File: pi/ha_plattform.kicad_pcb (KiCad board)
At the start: 2 copper layers, 54 x 55 mm, 15 parts, among them J3 Raspberry_Pi_2_3

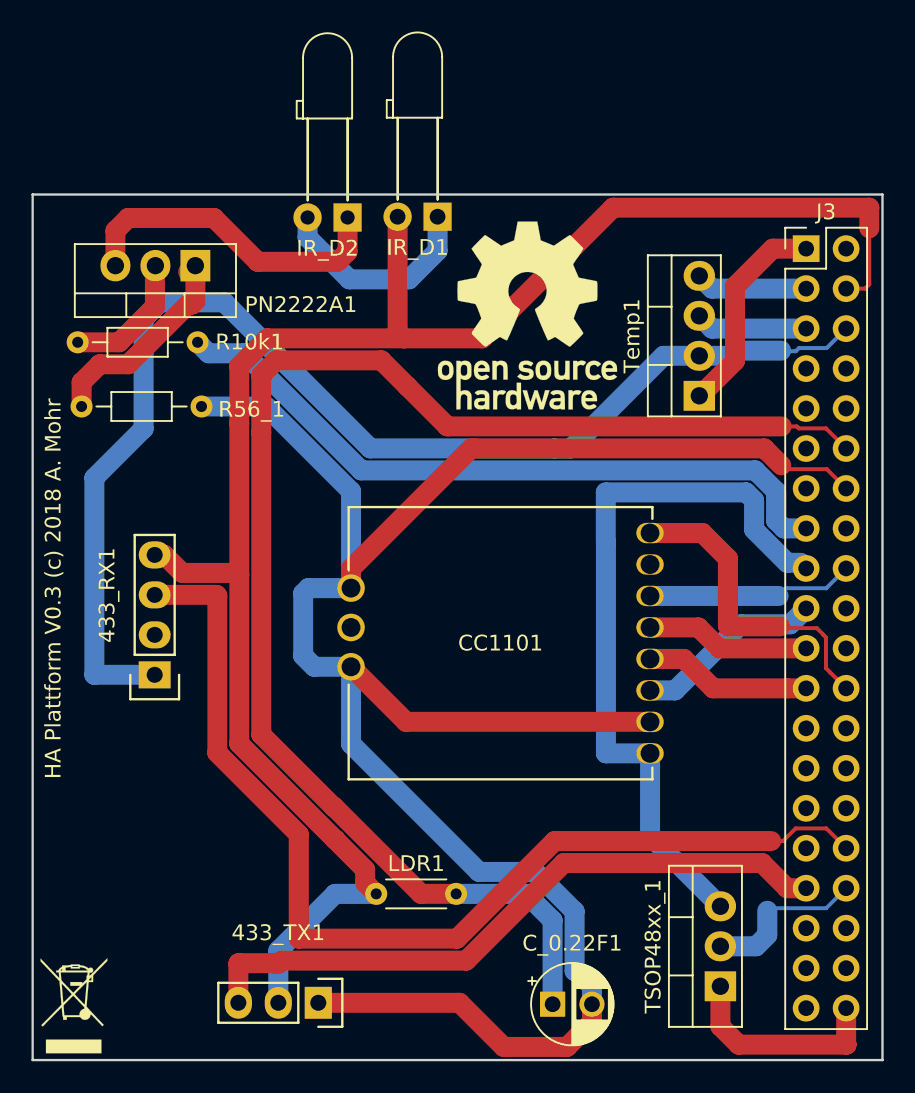
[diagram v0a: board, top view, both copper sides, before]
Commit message: Rerouted because footprints of 433mhz rx/tx were wrong-32-51.sch
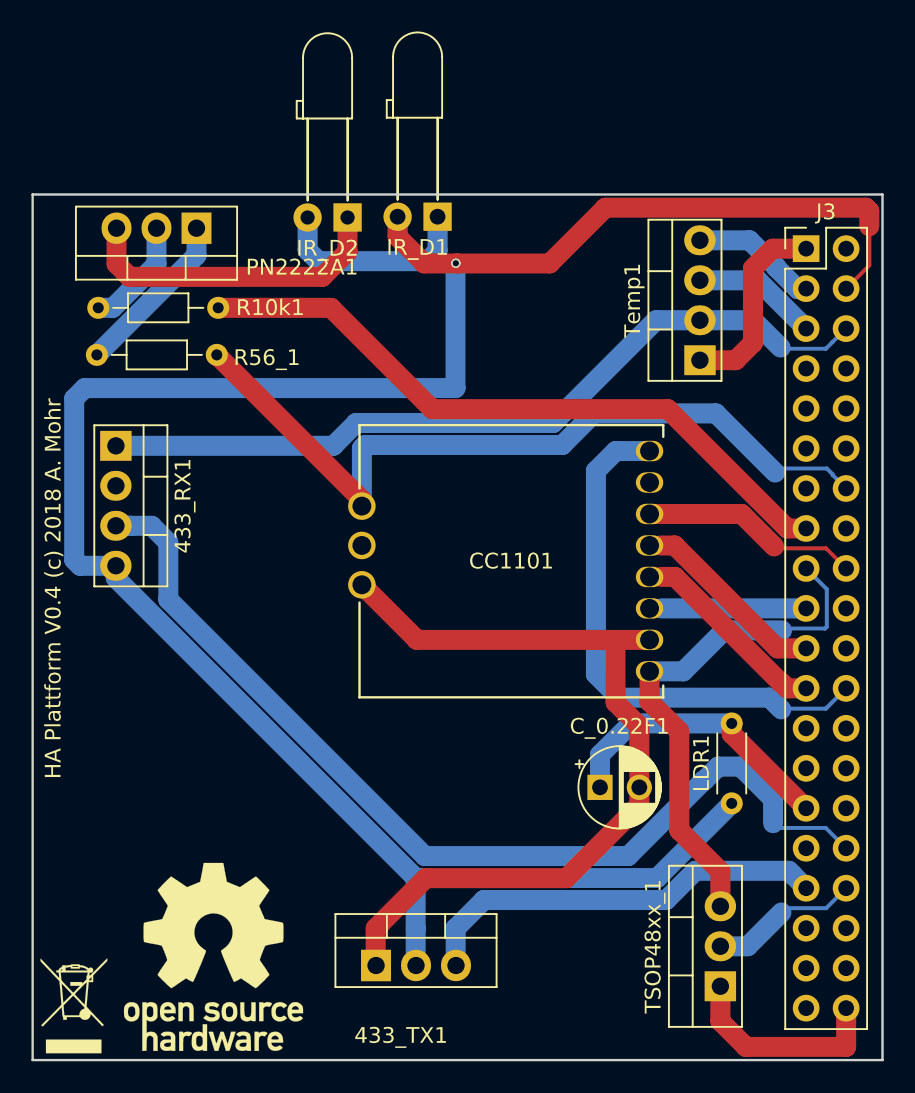
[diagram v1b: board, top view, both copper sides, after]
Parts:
- 433_RX1: footprint Sensors:RF_Receiver_433_MHz -> Package_TO_SOT_THT:TO-220-4_Vertical
- 433_TX1: footprint Sensors:RF_Transmitter_433_MHz -> Package_TO_SOT_THT:TO-220-3_Vertical
- moved REF** 45.4 mm to (31.5, 68.4)
- moved LDR1 23.3 mm to (64.4, 58.7), turned to 90 degrees
- moved C_0.22F1 14.1 mm to (56.0, 57.7)
- moved 433_RX1 9.80 mm to (25.3, 36.0), turned to 270 degrees
- moved 433_TX1 6.65 mm to (41.8, 69.0), turned to 0 degrees
- moved CC1101 5.26 mm to (50.4, 43.3)
- moved R56_1 3.42 mm to (24.1, 30.2)
- moved R10k1 2.55 mm to (31.8, 27.2)
- moved PN2222A1 2.38 mm to (30.4, 22.1)
- moved Temp1 2.26 mm to (62.4, 30.5)
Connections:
- 433_RX1 pad 2: Net-(433_RX1-Pad2) -> (no net)
- CC1101 pad 10: Net-(CC1101-Pad10) -> (no net)
- CC1101 pad 7: Net-(CC1101-Pad7) -> (no net)
- J3 pad 10: Net-(J3-Pad10) -> (no net)
- J3 pad 11: Net-(J3-Pad11) -> (no net)
- J3 pad 12: Net-(C_0.22F1-Pad1) -> (no net)
- J3 pad 13: Net-(J3-Pad13) -> (no net)
- J3 pad 16: Net-(J3-Pad16) -> (no net)
- J3 pad 2: Net-(J3-Pad2) -> (no net)
- J3 pad 20: Net-(J3-Pad20) -> (no net)
- J3 pad 22: Net-(J3-Pad22) -> (no net)
- J3 pad 25: Net-(J3-Pad25) -> (no net)
- J3 pad 26: Net-(J3-Pad26) -> (no net)
- J3 pad 27: Net-(J3-Pad27) -> (no net)
- J3 pad 28: Net-(J3-Pad28) -> (no net)
- J3 pad 29: Net-(J3-Pad29) -> Net-(C_0.22F1-Pad1)
- J3 pad 30: Net-(J3-Pad30) -> (no net)
- J3 pad 31: Net-(J3-Pad31) -> (no net)
- J3 pad 35: Net-(J3-Pad35) -> (no net)
- J3 pad 36: Net-(J3-Pad36) -> (no net)
- J3 pad 37: Net-(J3-Pad37) -> (no net)
- J3 pad 38: Net-(J3-Pad38) -> (no net)
- J3 pad 39: Net-(J3-Pad39) -> (no net)
- J3 pad 7: Net-(J3-Pad7) -> (no net)
- J3 pad 8: Net-(J3-Pad8) -> (no net)
- J3 pad 9: Net-(J3-Pad9) -> (no net)
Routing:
- net Net-(C_0.22F1-Pad1): track 92.1 -> 18.6 mm
- net Net-(433_TX1-Pad1): track 136.0 -> 104.3 mm
- net Net-(433_RX1-Pad1): track 79.9 -> 51.0 mm
- net Net-(433_RX1-Pad4): track 112.6 -> 139.0 mm, vias 0 -> 1
- net Net-(433_TX1-Pad3): track 41.9 -> 26.5 mm
- net Net-(CC1101-Pad8): track 20.2 -> 34.2 mm
- net Net-(CC1101-Pad1): track 46.8 -> 33.5 mm
- net Net-(PN2222A1-Pad1): track 13.8 -> 10.7 mm
- net Net-(433_RX1-Pad3): track 66.1 -> 63.2 mm
- net Net-(CC1101-Pad3): track 12.1 -> 9.23 mm
- net Net-(J3-Pad15): track 44.7 -> 43.2 mm
- net Net-(CC1101-Pad5): track 10.5 -> 11.9 mm
- net Net-(CC1101-Pad4): track 10.7 -> 12.2 mm
- net Net-(PN2222A1-Pad2): track 8.46 -> 7.13 mm
- net Net-(J3-Pad1): track 13.4 -> 12.5 mm
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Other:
- board text added: "HA Plattform V0.4 (c) 2018 A. Mohr"
- board text removed: "HA Plattform V0.3 (c) 2018 A. Mohr"
